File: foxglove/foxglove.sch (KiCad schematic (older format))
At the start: 62 parts, among them IC1 LFE5U-12F-6BG256C, J1 NEIGHBOR1, J2 NEIGHBOR2, J3 Conn_02x05_Odd_Even, J4 Conn_02x05_Odd_Even, J5 Conn_01x02_Female, J6 Conn_02x03_Odd_Even, J7 BONUS_ROW, U1 LM393, U2 ADP225, U25 74LVC1G53, U3 AP2127, U4 74LVC1G3157, U6 ADP225, U7 DAC084S085

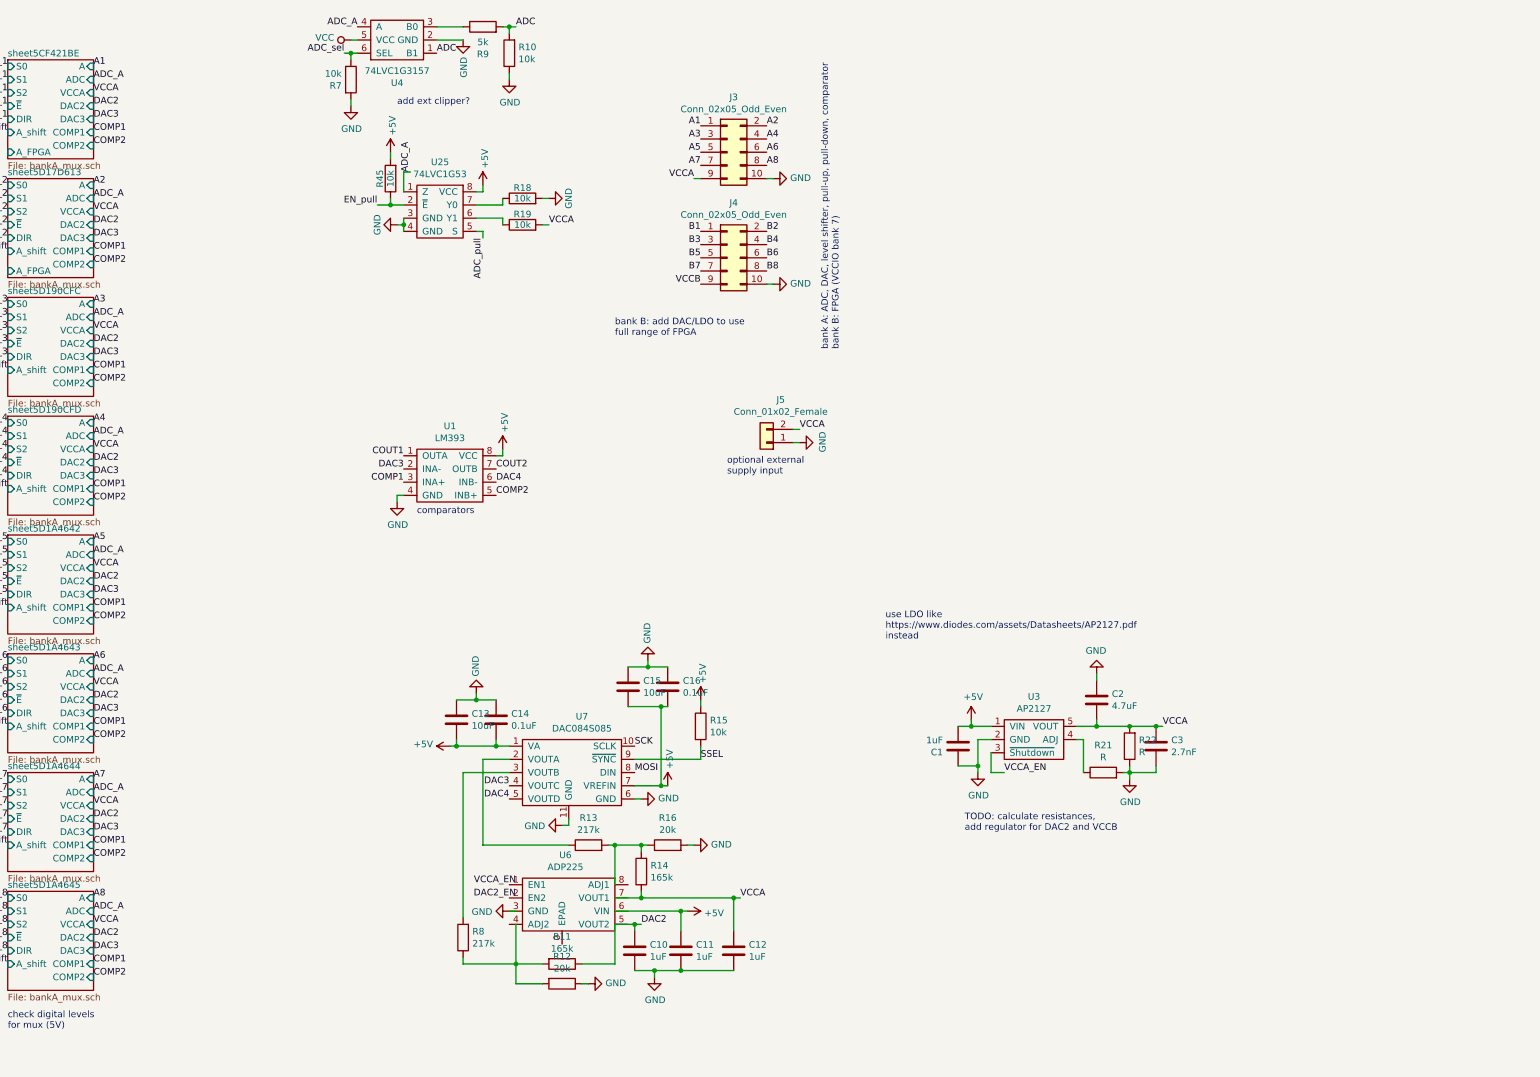
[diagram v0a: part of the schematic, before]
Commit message: Added DAC2 LDO
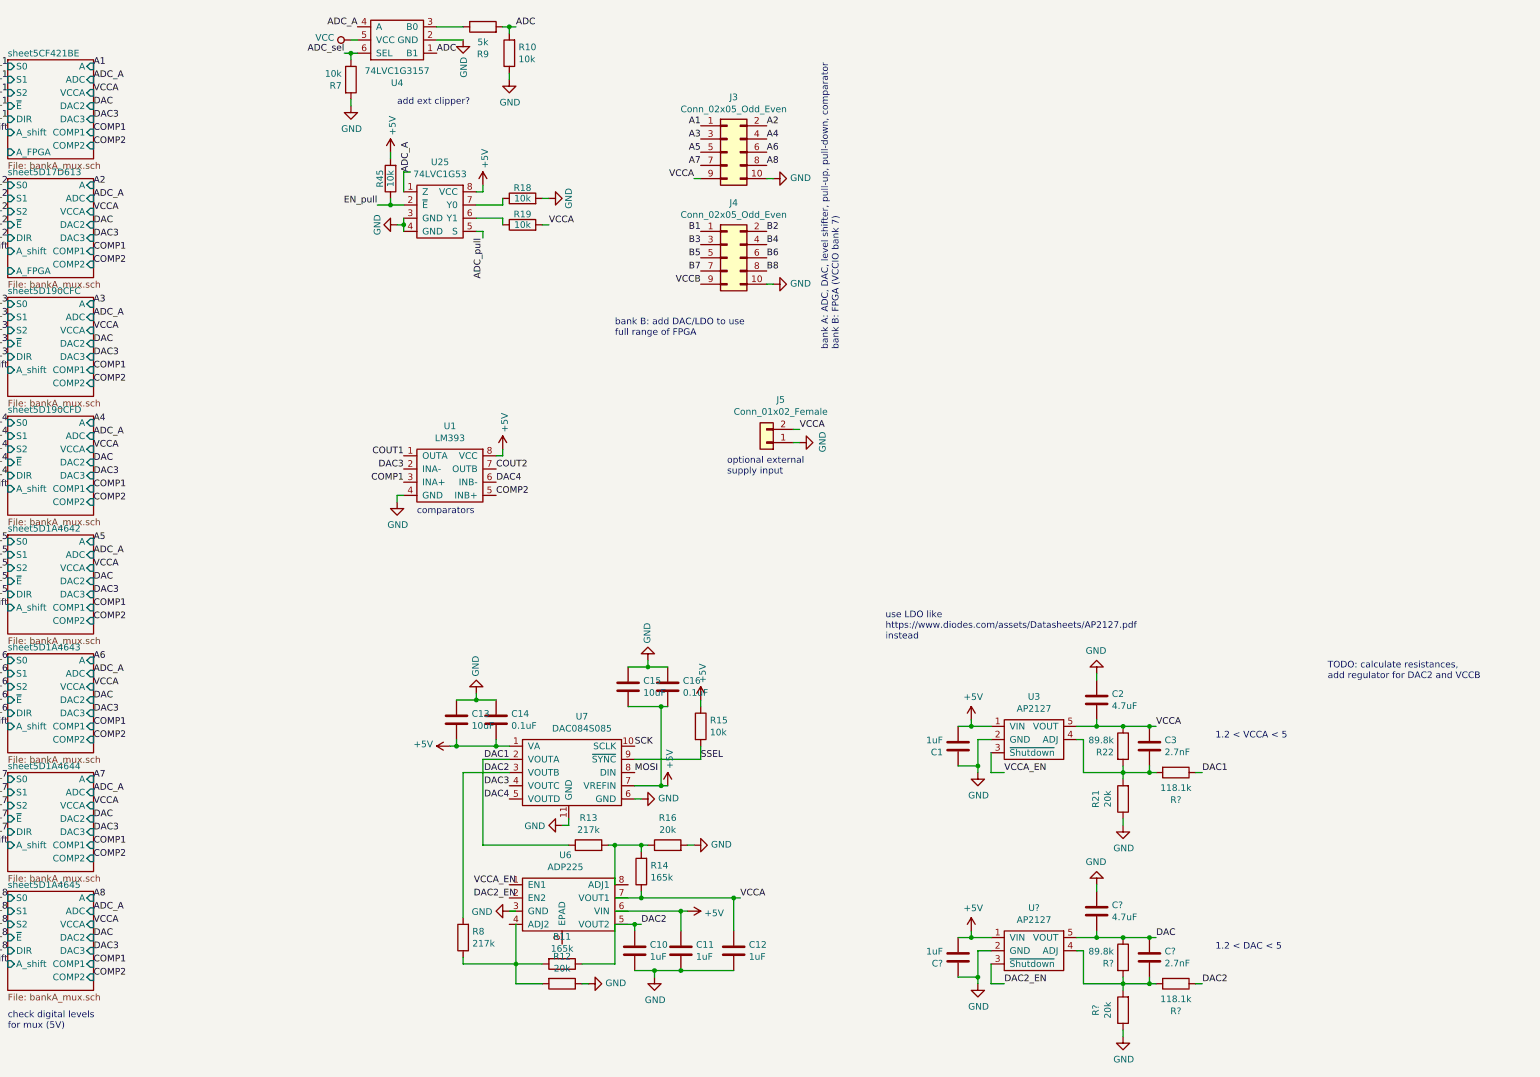
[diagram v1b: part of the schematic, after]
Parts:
- added C?: 1uF, gsg-modules:0402, symbol Device:C
- added C?: 2.7nF, symbol Device:C
- added C?: 4.7uF, symbol Device:C
- added R? (x2): 118.1k, symbol Device:R
- added R?: 20k, symbol Device:R
- added R?: 89.8k, symbol Device:R
- added U?: AP2127, Package_TO_SOT_SMD:SOT-23-5, symbol gsg-symbols:AP2127
- R21: value R -> 20k
- R22: value R -> 89.8k
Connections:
- net labels added: DAC, DAC1
- wire segments 349 -> 377
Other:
- note added: "1.2 < DAC < 5"
- note added: "1.2 < VCCA < 5"
- moved on the sheet: C3, R21, R22

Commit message: Added LDOs for DAC and VCCB
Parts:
- removed C11: 1uF, gsg-modules:0402, symbol Device:C
- removed R11, R14: 165k, gsg-modules:0402, symbol Device:R
- removed R16: 20k, gsg-modules:0402, symbol Device:R
- removed R8: 217k, gsg-modules:0402, symbol Device:R
- removed U6: ADP225, Package_CSP:LFCSP-8_2x2mm_P0.5mm, symbol gsg-symbols:ADP225
- added C8: 1uF, gsg-modules:0402, symbol Device:C
- added R63: 127.2k, symbol Device:R
- added U6: AP2127, Package_TO_SOT_SMD:SOT-23-5, symbol gsg-symbols:AP2127
- C10: value 1uF -> 4.7uF; footprint gsg-modules:0402 -> (none); Description CAP CER 1UF 25V X5R 0402 -> (none); Manufacturer Murata Electronics North America -> (none); Part Number GRT155R61E105KE01D -> (none)
- C12: value 1uF -> 2.7nF; footprint gsg-modules:0402 -> (none); Description CAP CER 1UF 25V X5R 0402 -> (none); Manufacturer Murata Electronics North America -> (none); Part Number GRT155R61E105KE01D -> (none)
- J6: footprint gsg-modules:HEADER-2x3 -> Connector_PinHeader_1.00mm:PinHeader_2x03_P1.00mm_Vertical_SMD
- R12: value 20k -> 57.25k; footprint gsg-modules:0402 -> (none)
- R13: value 217k -> 20k; footprint gsg-modules:0402 -> (none)
- gave numbers to parts that had none: 8
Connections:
- net labels added: VCCB_EN
- wire segments 377 -> 366
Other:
- note added: "1.14 <VCCB < 3.465"
- note added: "1.1V, 2.5V power supplies"
- note added: "ADC pull up/down"
- note added: "ADC voltage divider"
- note removed: "TODO: calculate resistances,\nadd regulator for DAC2 and VCCB"
- note removed: "TODO: standard JTAG header?"
- note removed: "bank B: add DAC/LDO to use\nfull range of FPGA"
- note removed: "https://github.com/tinyfpga/TinyFPGA-EX/tree/master/board\n"
- note removed: "use LDO like \nhttps://www.diodes.com/assets/Datasheets/AP2127.pdf\ninstead"
- moved on the sheet: C1, C11, C13, C14, C15, C16, C2, C3, C4, C5, C6, C7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

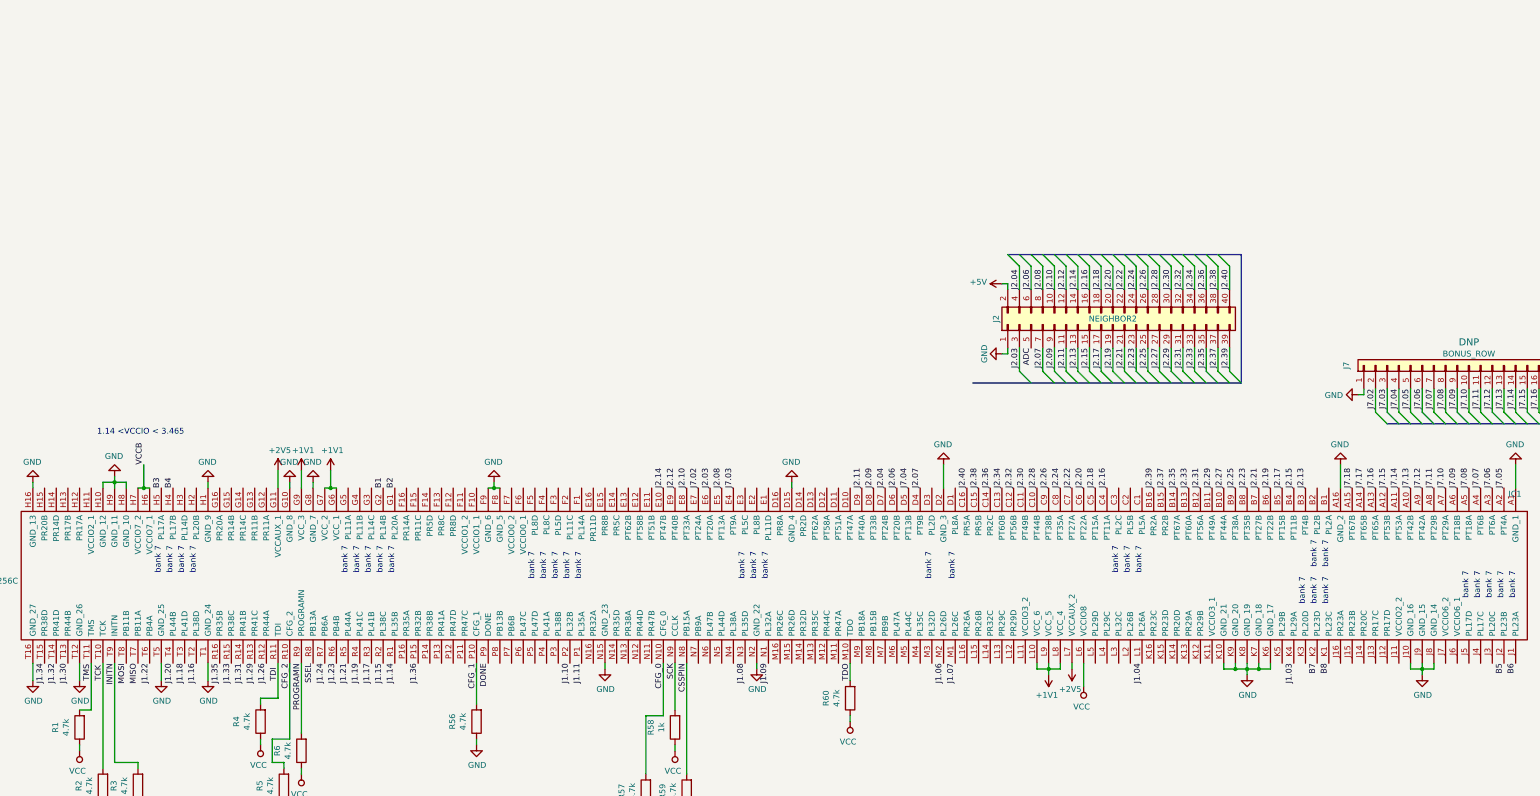
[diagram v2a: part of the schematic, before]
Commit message: Routed bank B to FPGA VCCIO7, added bypass caps
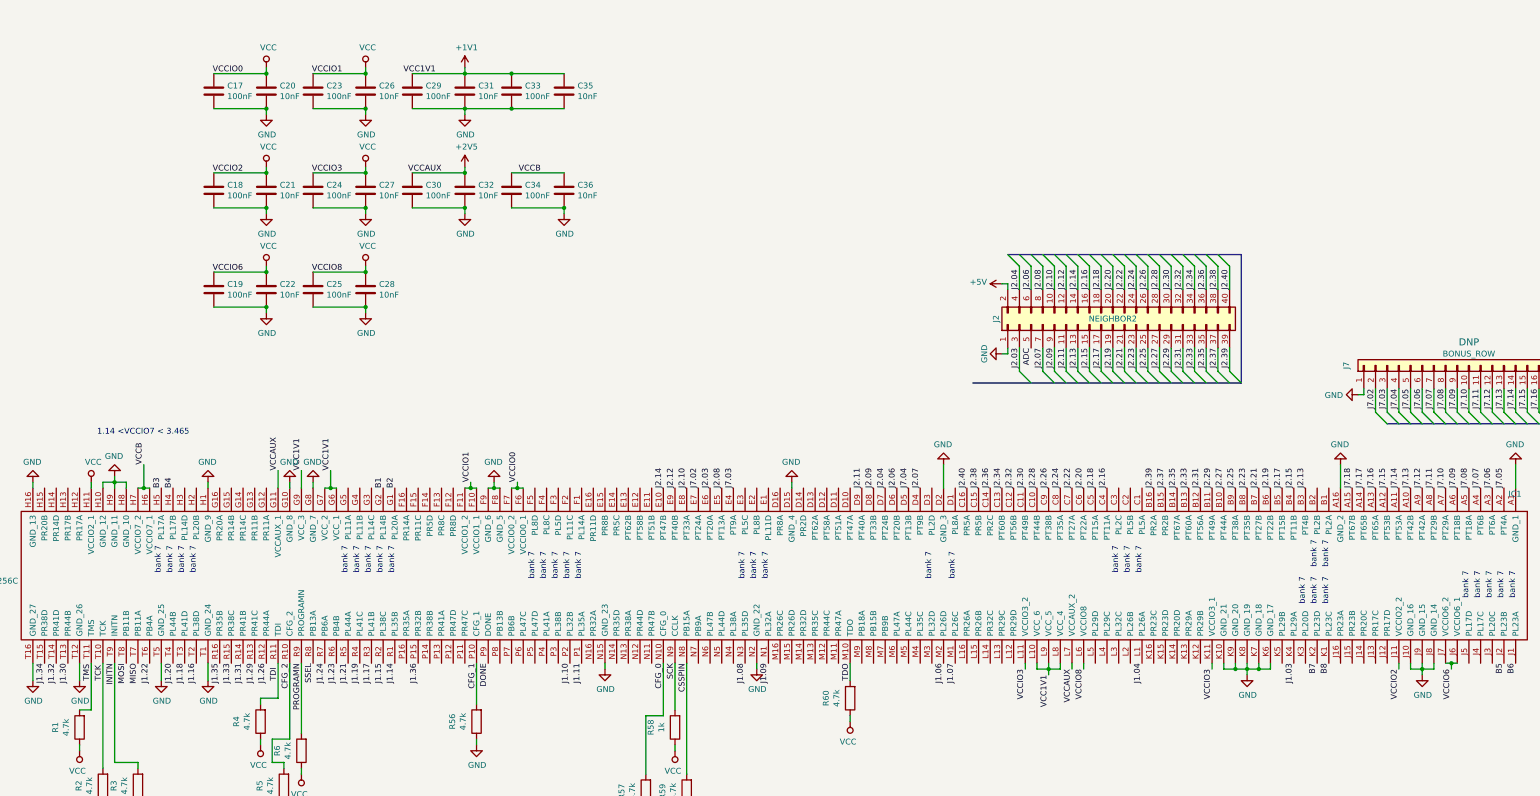
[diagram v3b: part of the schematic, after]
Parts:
- added C17, C18, C19, C23, C24, C25, C29, C30, C33, C34: 100nF, gsg-modules:0402, symbol Device:C
- added C20, C21, C22, C26, C27, C28, C31, C32, C35, C36: 10nF, gsg-modules:0402, symbol Device:C
- C10, C11, C12, C2, C3, C9, R11, R12, R13, R14, R16, R21, R22, R63, R8: footprint (none) -> gsg-modules:0402
- U1: footprint (none) -> gsg-modules:SOIC8-154
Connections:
- net +1V1: now also C29.1, C31.1, C33.1, C35.1
- net +2V5: now also C30.1, C32.1
- net GND: now also C17.2, C18.2, C19.2, C20.2, C21.2, C22.2, C23.2, C24.2, C25.2, C26.2, C27.2, C28.2, C29.2, C30.2, C31.2, C32.2, C33.2, C34.2, C35.2, C36.2
- net VCC: now also IC1.F10 (VCCIO1_1), IC1.F11 (VCCIO1_2), IC1.F6 (VCCIO0_1), IC1.F7 (VCCIO0_2), IC1.H11 (VCCIO2_1), IC1.J11 (VCCIO2_2), IC1.J6 (VCCIO6_1), IC1.J7 (VCCIO6_2), IC1.K11 (VCCIO3_1), IC1.L11 (VCCIO3_2), C17.1, C18.1, C19.1, C20.1, C21.1, C22.1, C23.1, C24.1, C25.1, C26.1, C27.1, C28.1
- net VCCB: now also C34.1, C36.1
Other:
- note added: "1.14 <VCCIO7 < 3.465"
- note removed: "1.14 <VCCIO < 3.465"
